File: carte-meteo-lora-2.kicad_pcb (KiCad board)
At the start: 4 copper layers, 50 x 50 mm, 79 parts, among them J1 USB_C_Receptacle_USB2.0_14P, J2 Conn_Coaxial, J3 Conn_Coaxial, J4 Conn_Coaxial, J5 Conn_01x04_Pin, SW1 SW_Push, SW2 SW_Push, U1 HS96L03W2C03, U2 SX1262TR8-GC, U3 LDL212PV33R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

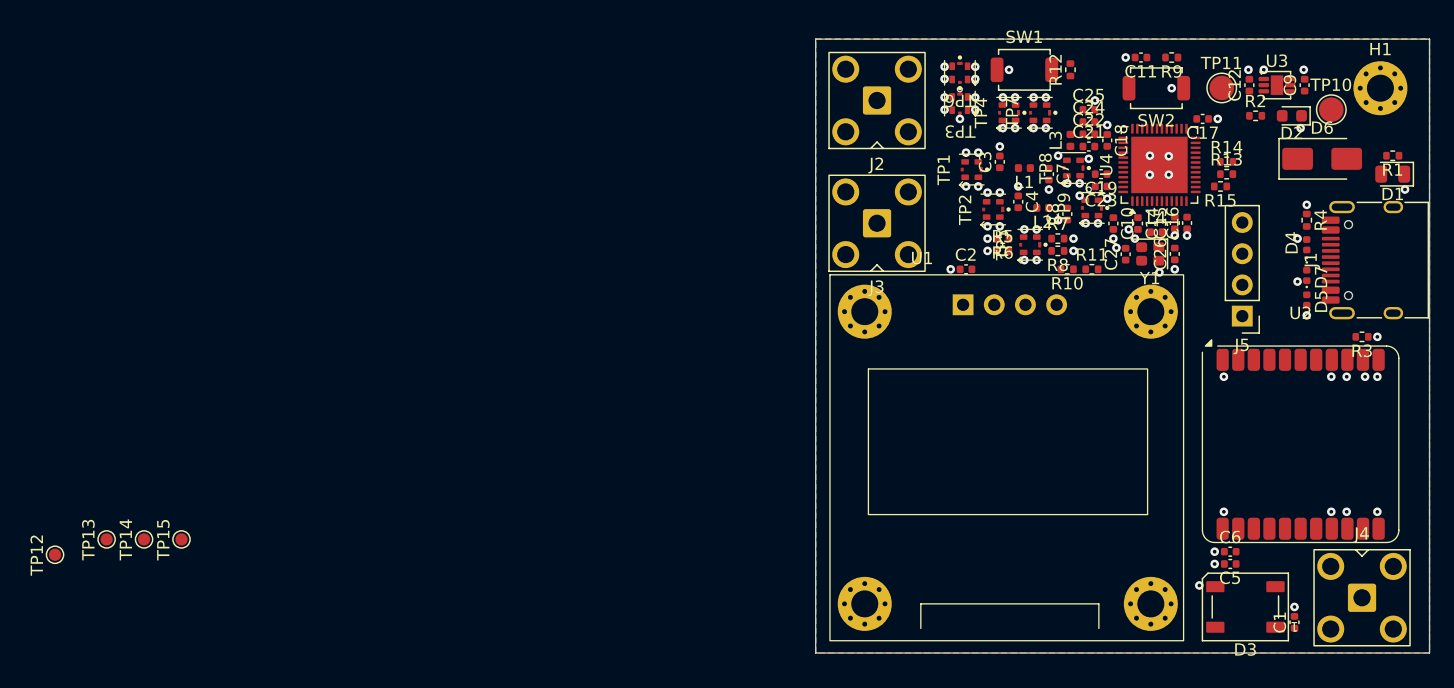
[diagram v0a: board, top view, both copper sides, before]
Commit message: pcb: reorganize programmable gpios
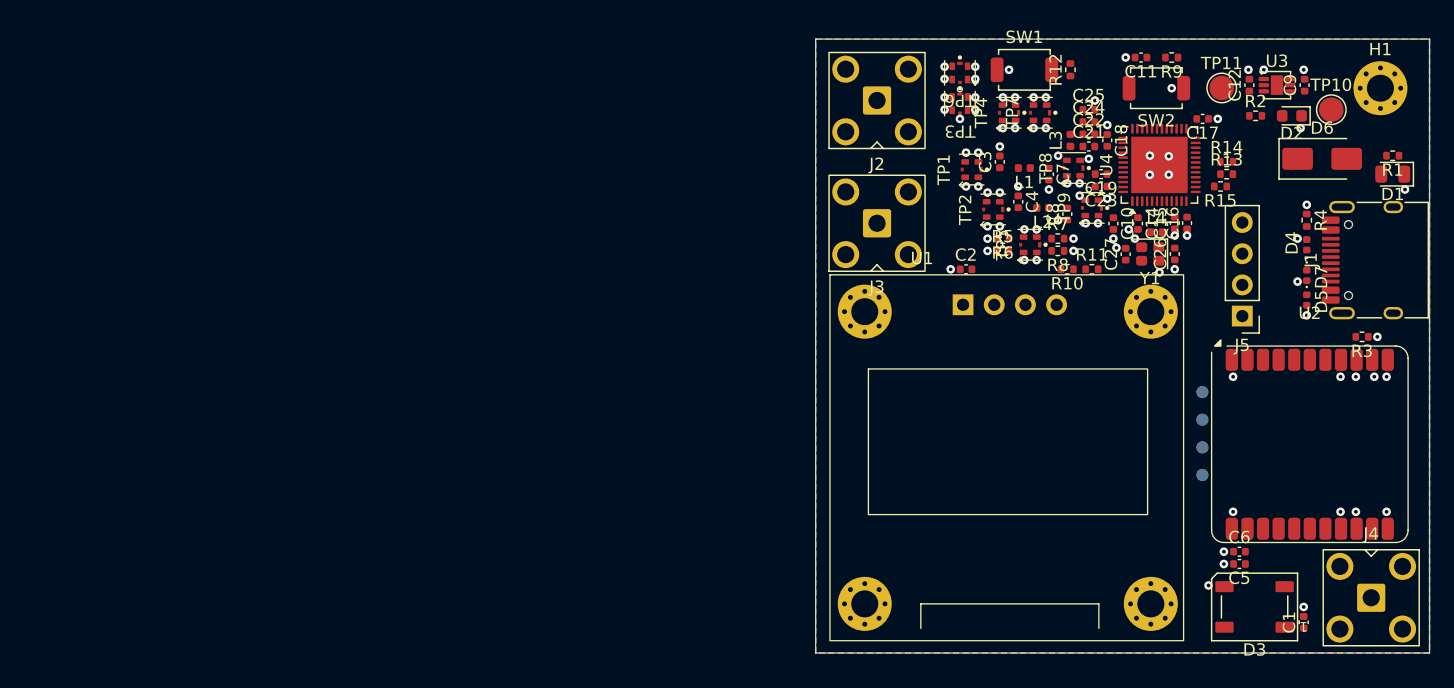
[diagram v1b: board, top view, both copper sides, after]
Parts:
- TP12, TP13, TP14, TP15: moved to B.Cu
- moved TP12 93.7 mm to (125.5, 64.5), turned to 0 degrees
- moved TP13 90.1 mm to (125.5, 57.8), turned to 0 degrees
- moved TP14 86.5 mm to (125.5, 62.2), turned to 0 degrees
- moved TP15 83.7 mm to (125.5, 60.0), turned to 0 degrees
- moved C5 0.75 mm to (128.5, 71.8)
- moved C6 0.75 mm to (128.5, 70.8)
- moved C1 0.75 mm to (133.8, 76.5)
- moved D3 0.75 mm to (129.8, 75.2)
- moved J4 0.75 mm to (139.2, 74.5)
- moved U2 0.75 mm to (134.2, 62.0)
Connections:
- U4 pad 17: /RGB1 -> /BUSY
- U4 pad 18: /RST -> /DIO3
- U4 pad 19: /BUSY -> /DIO1
- U4 pad 33: /DIO1 -> /RST
- U4 pad 34: /DIO3 -> /RGB1

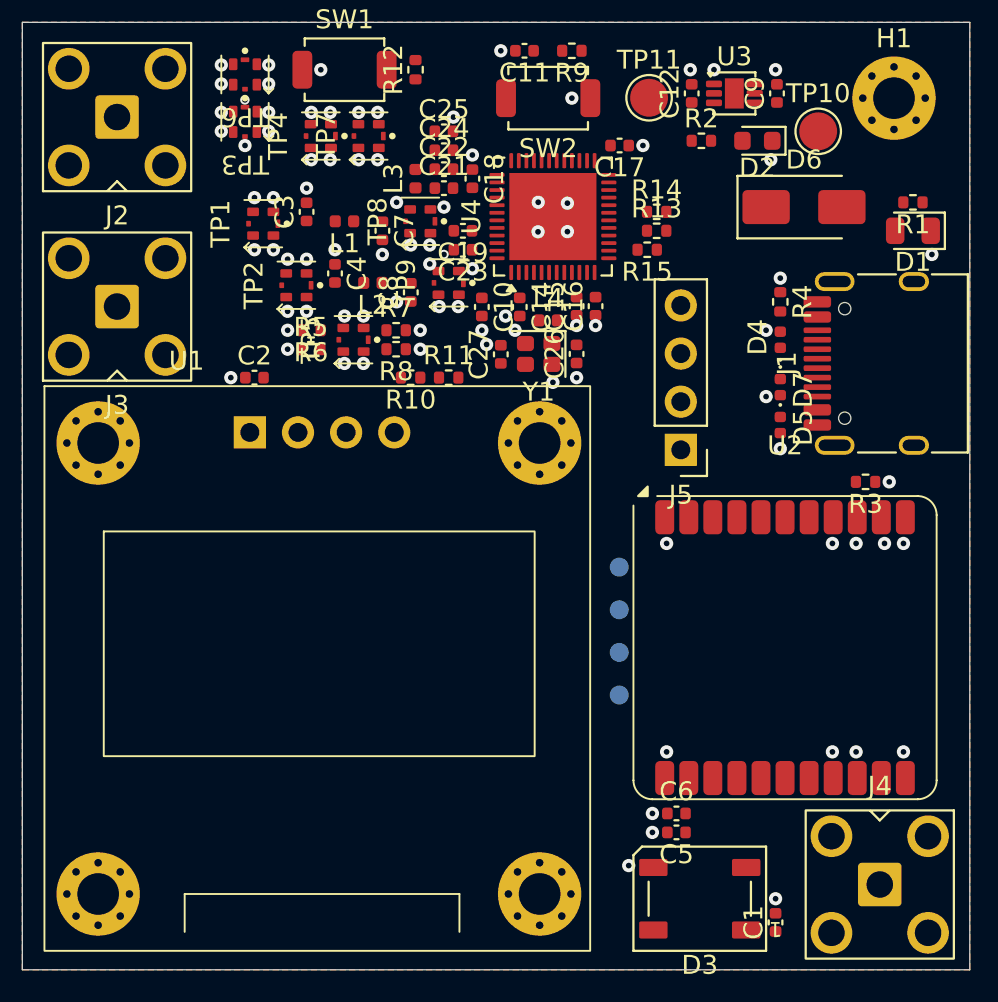
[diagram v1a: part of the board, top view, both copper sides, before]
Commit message: pcb: add rf routing
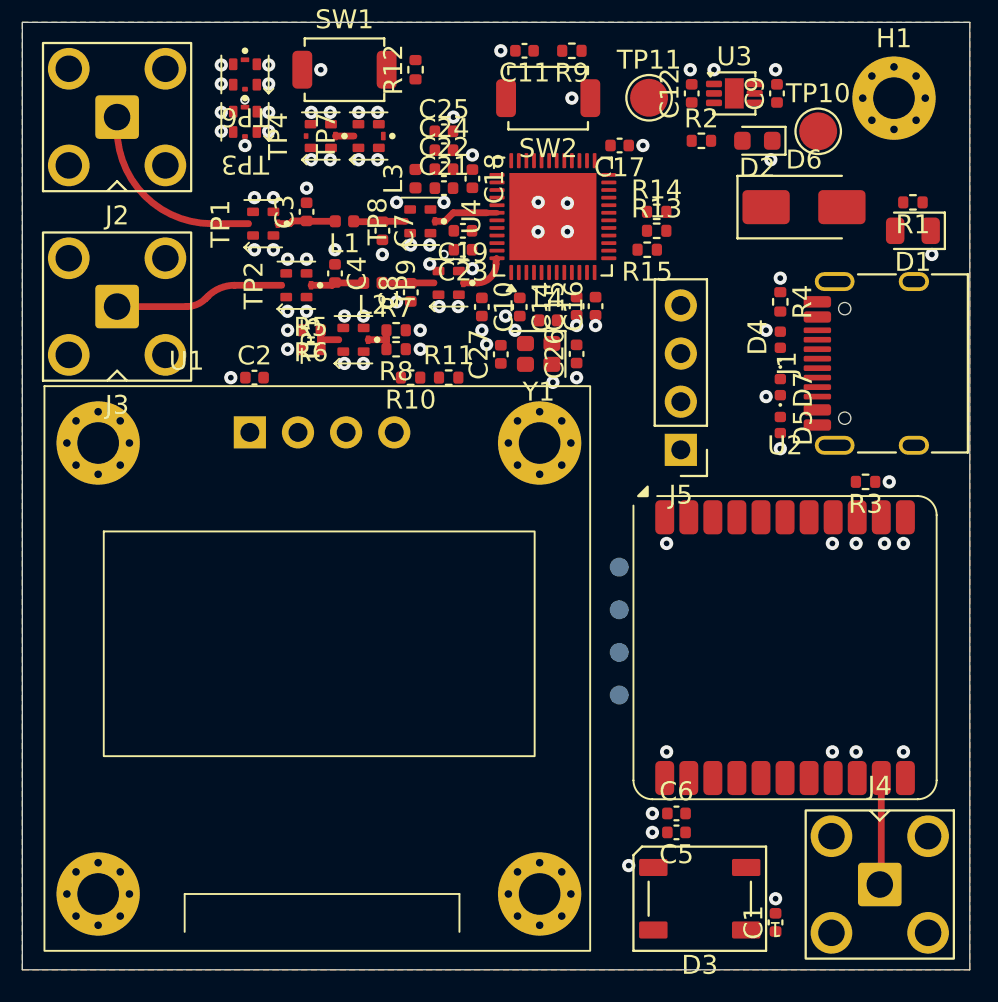
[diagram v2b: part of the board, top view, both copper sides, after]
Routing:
- net /RF_CN_2G: track 0.00 -> 10.2 mm
- net /RF_CN_5G: track 0.00 -> 8.99 mm
- net /RF_LR: track 0.00 -> 5.65 mm
- net /ANT_2G: track 0.00 -> 3.46 mm
- net /RF_TRANS_2G: track 0.00 -> 3.10 mm
- net /RF_TRANS_5G: track 0.00 -> 2.85 mm
- net /RF_ESP_5G: track 0.00 -> 2.76 mm
- net /RF_ESP_2G: track 0.00 -> 2.76 mm
- net /ANT_5G: track 0.00 -> 2.56 mm
- net Net-(R5-Pad2): track 0.00 -> 1.97 mm
- net Net-(R7-Pad1): track 0.00 -> 1.97 mm
- net Net-(TP4-PadI): track 0.00 -> 0.97 mm

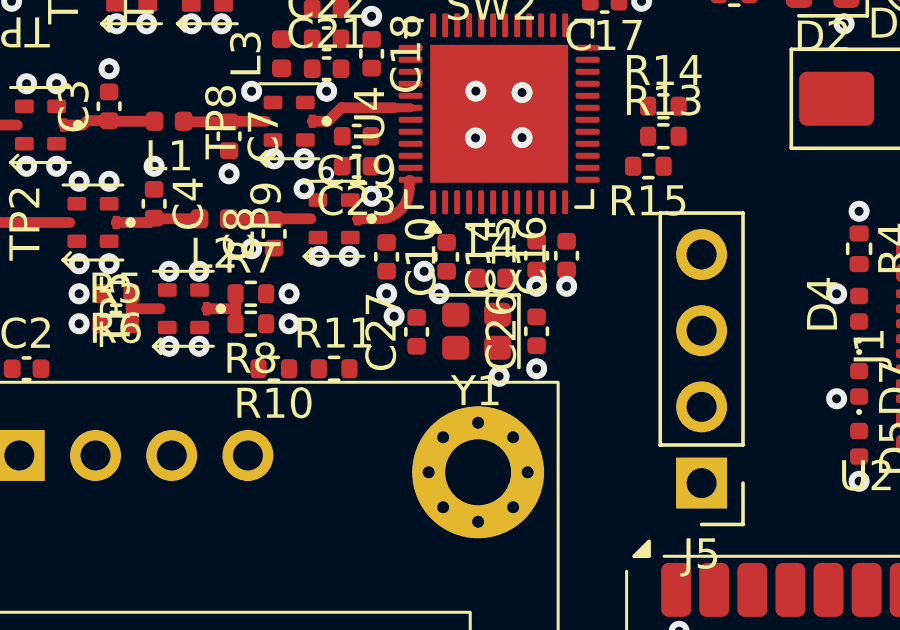
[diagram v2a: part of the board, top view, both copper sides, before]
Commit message: pcb: add crystal routing
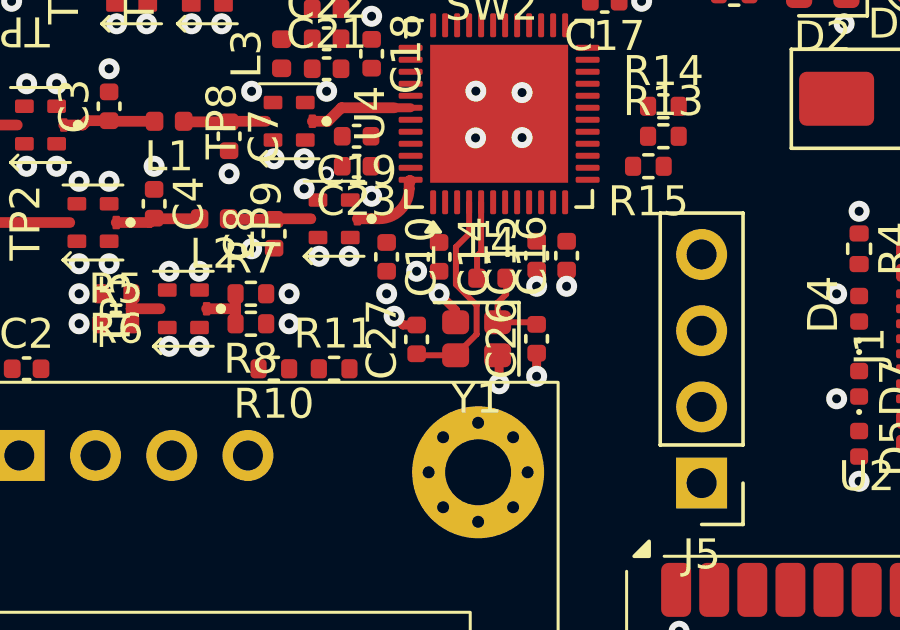
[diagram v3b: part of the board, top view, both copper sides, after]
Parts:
- moved C14 0.25 mm to (120.0, 44.0)
- moved C26 0.25 mm to (123.2, 46.8)
- moved C27 0.25 mm to (119.2, 46.8)
- moved Y1 0.25 mm to (121.2, 46.8)
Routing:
- net /XTAL_N: track 0.00 -> 7.18 mm
- net GND: track 0.00 -> 3.79 mm
- net /XTAL_PL: track 0.00 -> 2.92 mm
- net /XTAL_P: track 0.00 -> 2.59 mm
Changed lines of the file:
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@@
 	(footprint "Crystal:Crystal_SMD_2016-4Pin_2.0x1.6mm"
 		(layer "F.Cu")
-		(at 121.25 46.5 180)
+		(at 121.25 46.75 180)
 		(descr "SMD2016/4, Crystal, 2.0x1.6mm package, SMD, http://www.q-crystal.com/upload/5/2015552223166229.pdf")
 		(property "Reference" "Y1"
@@
 	(footprint "Capacitor_SMD:C_0402_1005Metric"
 		(layer "F.Cu")
-		(at 120.25 44.02 -90)
+		(at 120 44.02 -90)
 		(descr "Capacitor SMD 0402 (1005 Metric), square (rectangular) end terminal, IPC-7351 nominal, (Body size source: IPC-SM-782 page 76, https://www.pcb-3d.com/wordpress/wp-content/uploads/ipc-sm-782a_amendment_1_and_2.pdf)")
 		(tags "capacitor")
@@
 	(footprint "Capacitor_SMD:C_0402_1005Metric"
 		(layer "F.Cu")
-		(at 123.25 46.5 90)
+		(at 123.25 46.75 90)
 		(descr "Capacitor SMD 0402 (1005 Metric), square (rectangular) end terminal, IPC-7351 nominal, (Body size source: IPC-SM-782 page 76, https://www.pcb-3d.com/wordpress/wp-content/uploads/ipc-sm-782a_amendment_1_and_2.pdf)")
 		(tags "capacitor")
@@
 	(footprint "Capacitor_SMD:C_0402_1005Metric"
 		(layer "F.Cu")
-		(at 119.25 46.52 90)
+		(at 119.25 46.77 90)
 		(descr "Capacitor SMD 0402 (1005 Metric), square (rectangular) end terminal, IPC-7351 nominal, (Body size source: IPC-SM-782 page 76, https://www.pcb-3d.com/wordpress/wp-content/uploads/ipc-sm-782a_amendment_1_and_2.pdf)")
 		(tags "capacitor")
@@
 		(layer "Edge.Cuts")
 	)
+	(segment
+		(start 120.55 45.8)
+		(end 120 45.25)
+		(width 0.3)
+		(layer "F.Cu")
+		(net "GND")
+	)
+	(segment
+		(start 119.25 46.29)
+		(end 118.79 46.29)
+		(width 0.3)
+		(layer "F.Cu")
+		(net "GND")
+	)
+	(segment
+		(start 118.79 46.29)
+		(end 118.5 46)
+		(width 0.3)
+		(layer "F.Cu")
+		(net "GND")
+	)
+	(segment
+		(start 122 48.25)
+		(end 122 47.35)
+		(width 0.3)
+		(layer "F.Cu")
+		(net "GND")
+	)
+	(segment
+		(start 122 47.35)
+		(end 121.95 47.3)
+		(width 0.3)
+		(layer "F.Cu")
+		(net "GND")
+	)
+	(segment
+		(start 120.55 46.2)
+		(end 120.55 45.8)
+		(width 0.3)
+		(layer "F.Cu")
+		(net "GND")
+	)
+	(segment
+		(start 123.25 47.23)
+		(end 123.25 48)
+		(width 0.3)
+		(layer "F.Cu")
+		(net "GND")
+	)
 	(via
 		(at 133.5 36.25)
@@
 	)
 	(via
-		(at 122 48)
+		(at 122 48.25)
 		(size 0.7)
 		(drill 0.3)
@@
 	)
 	(via
-		(at 119.5 44.5)
+		(at 119.25 44.5)
 		(size 0.7)
 		(drill 0.3)
@@
 	)
 	(via
-		(at 123.25 47.75)
+		(at 123.25 48)
 		(size 0.7)
 		(drill 0.3)
@@
 	)
 	(segment
+		(start 121 42.2)
+		(end 121 43.25)
+		(width 0.2)
+		(layer "F.Cu")
+		(net "/XTAL_N")
+	)
+	(segment
+		(start 120.56 43.69)
+		(end 120.56 44.940001)
+		(width 0.2)
+		(layer "F.Cu")
+		(net "/XTAL_N")
+	)
+	(segment
+		(start 120.56 44.940001)
+		(end 121.25 45.630001)
+		(width 0.2)
+		(layer "F.Cu")
+		(net "/XTAL_N")
+	)
+	(segment
+		(start 121 43.25)
+		(end 120.56 43.69)
+		(width 0.2)
+		(layer "F.Cu")
+		(net "/XTAL_N")
+	)
+	(segment
+		(start 119.3 47.3)
+		(end 119.25 47.25)
+		(width 0.2)
+		(layer "F.Cu")
+		(net "/XTAL_N")
+	)
+	(segment
+		(start 120.55 47.3)
+		(end 119.3 47.3)
+		(width 0.2)
+		(layer "F.Cu")
+		(net "/XTAL_N")
+	)
+	(segment
+		(start 121.25 46.6)
+		(end 120.55 47.3)
+		(width 0.2)
+		(layer "F.Cu")
+		(net "/XTAL_N")
+	)
+	(segment
+		(start 121.25 45.630001)
+		(end 121.25 46.6)
+		(width 0.2)
+		(layer "F.Cu")
+		(net "/XTAL_N")
+	)
+	(segment
+		(start 121.265 44.73)
+		(end 121.265 43.985)
+		(width 0.2)
+		(layer "F.Cu")
+		(net "/XTAL_P")
+	)
+	(segment
+		(start 121.4 42.2)
+		(end 121.4 43.85)
+		(width 0.2)
+		(layer "F.Cu")
+		(net "/XTAL_P")
+	)
+	(segment
+		(start 121.4 43.85)
+		(end 121.265 43.985)
+		(width 0.2)
+		(layer "F.Cu")
+		(net "/XTAL_P")
+	)
+	(segment
 		(start 119.05 39.05)
 		(end 118.51192 39.05)
@@
 	)
 	(segment
+		(start 123.18 46.2)
+		(end 123.25 46.27)
+		(width 0.2)
+		(layer "F.Cu")
+		(net "/XTAL_PL")
+	)
+	(segment
+		(start 121.95 46.2)
+		(end 121.95 45.55)
+		(width 0.2)
+		(layer "F.Cu")
+		(net "/XTAL_PL")
+	)
+	(segment
+		(start 122.235 45.265)
+		(end 122.235 44.73)
+		(width 0.2)
+		(layer "F.Cu")
+		(net "/XTAL_PL")
+	)
+	(segment
+		(start 121.95 45.55)
+		(end 122.235 45.265)
+		(width 0.2)
+		(layer "F.Cu")
+		(net "/XTAL_PL")
+	)
+	(segment
+		(start 121.95 46.2)
+		(end 123.18 46.2)
+		(width 0.2)
+		(layer "F.Cu")
+		(net "/XTAL_PL")
+	)
+	(segment
 		(start 139.33 74.42)
 		(end 139.25 74.5)
@@
 	)
 	(zone
+		(layer "F.Cu")
+		(hatch edge 0.5)
+		(connect_pads
+			(clearance 0)
+		)
+		(min_thickness 0.25)
+		(keepout
+			(tracks allowed)
+			(vias allowed)
+			(pads allowed)
+			(copperpour not_allowed)
+			(footprints allowed)
+		)
+		(placement
+			(enabled no)
+			(sheetname "/")
+		)
+		(fill
+			(thermal_gap 0.5)
+			(thermal_bridge_width 0.5)
+			(island_removal_mode 0)
+		)
+		(polygon
+			(pts
+				(xy 123 44.25) (xy 123.75 45) (xy 123.75 47.75) (xy 123.25 48.25) (xy 119.25 48.25) (xy 118.75 47.75)
+				(xy 118.75 45.75) (xy 120.25 44.25)
+			)
+		)
+	)
+	(zone

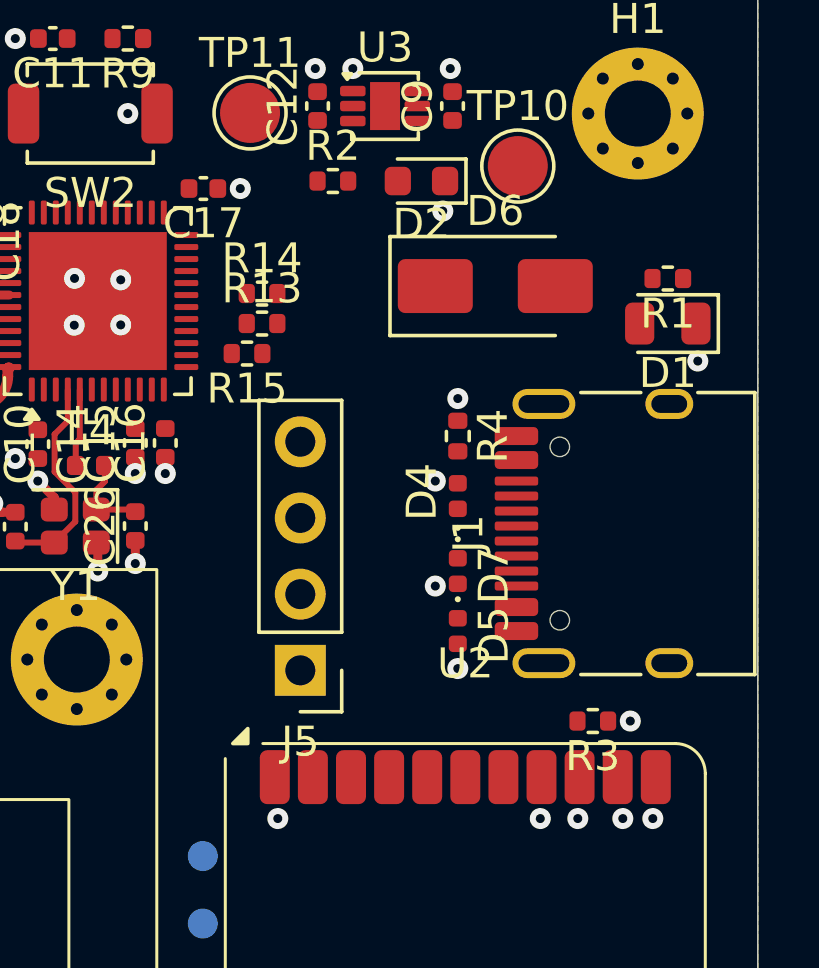
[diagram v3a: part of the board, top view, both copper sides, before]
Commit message: pcb: add usb routing
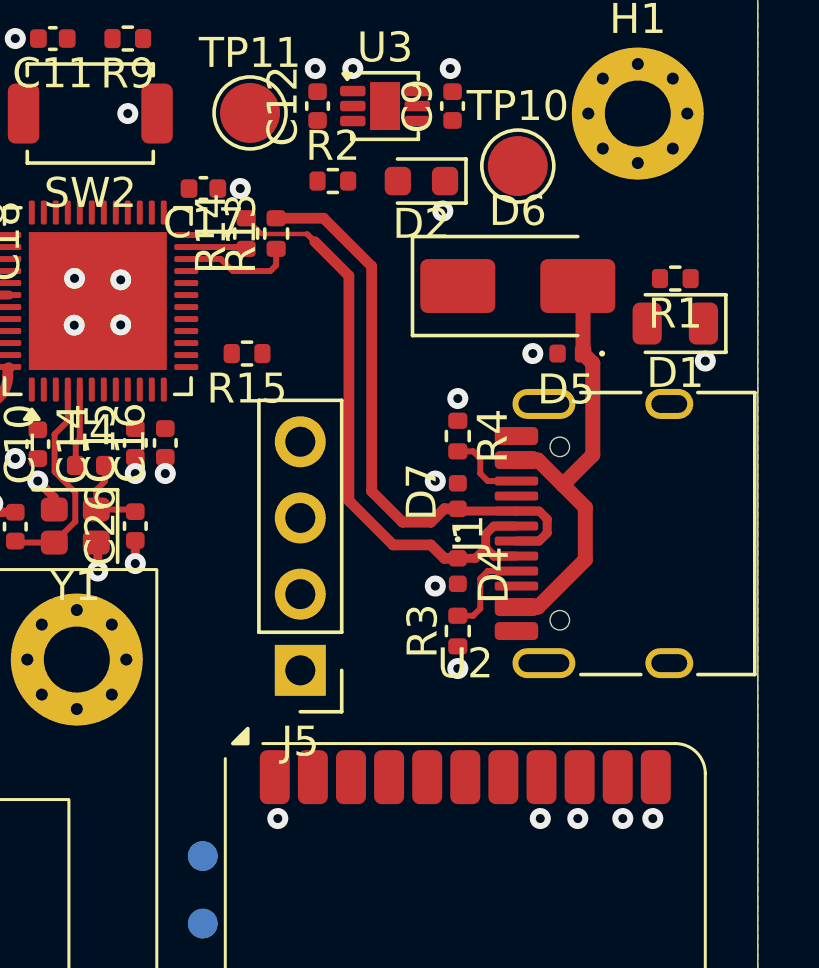
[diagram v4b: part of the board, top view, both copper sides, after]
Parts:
- moved D5 9.98 mm to (137.8, 41.0), turned to 180 degrees
- moved R3 5.41 mm to (134.0, 50.2), turned to 90 degrees
- moved R13 3.04 mm to (127.9, 37.0), turned to 90 degrees
- moved D4 2.50 mm to (134.0, 48.2), turned to -90 degrees
- moved D7 2.50 mm to (134.0, 45.8), turned to 90 degrees
- moved R14 2.07 mm to (126.9, 37.0), turned to 90 degrees
- moved D6 0.75 mm to (136.0, 38.8)
- moved D1 0.25 mm to (141.2, 40.0)
- moved R1 0.25 mm to (141.2, 38.5)
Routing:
- net /D-: track 0.00 -> 20.0 mm
- net /D+: track 0.00 -> 19.6 mm
- net +Vbus: track 0.00 -> 14.9 mm
- net /ESP_D+: track 0.00 -> 3.79 mm
- net Net-(J1-CC1): track 0.00 -> 3.16 mm
- net Net-(J1-CC2): track 0.00 -> 2.66 mm
- net /ESP_D-: track 0.00 -> 2.02 mm
